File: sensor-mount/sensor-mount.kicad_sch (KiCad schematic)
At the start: 6 parts, among them J1 Conn_01x02, J2 Conn_01x02, U1 MAX31725

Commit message: The Maxim footprint has 0.65mm pitch.
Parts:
- U1: footprint Package_DFN_QFN:TDFN-8-1EP_3x2mm_P0.5mm_EP1.80x1.65mm_ThermalVias -> maxim-8tdfn-vias:DFN-8-1EP_3x3mm_P0.65mm_EP1.7x2.05mm
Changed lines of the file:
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@@
     (property "Reference" "U1" (id 0) (at 134.62 87.63 0))
     (property "Value" "MAX31725" (id 1) (at 134.62 81.28 0))
-    (property "Footprint" "Package_DFN_QFN:TDFN-8-1EP_3x2mm_P0.5mm_EP1.80x1.65mm_ThermalVias" (id 2) (at 134.62 87.63 0)
+    (property "Footprint" "maxim-8tdfn-vias:DFN-8-1EP_3x3mm_P0.65mm_EP1.7x2.05mm" (id 2) (at 134.62 87.63 0)
       (effects (font (size 1.27 1.27)) hide)
     )
@@
     )
     (path "/1ccf6312-fd46-4669-9722-1b0a94926d20"
-      (reference "U1") (unit 1) (value "MAX31725") (footprint "Package_DFN_QFN:TDFN-8-1EP_3x2mm_P0.5mm_EP1.80x1.65mm_ThermalVias")
+      (reference "U1") (unit 1) (value "MAX31725") (footprint "maxim-8tdfn-vias:DFN-8-1EP_3x3mm_P0.65mm_EP1.7x2.05mm")
     )
   )

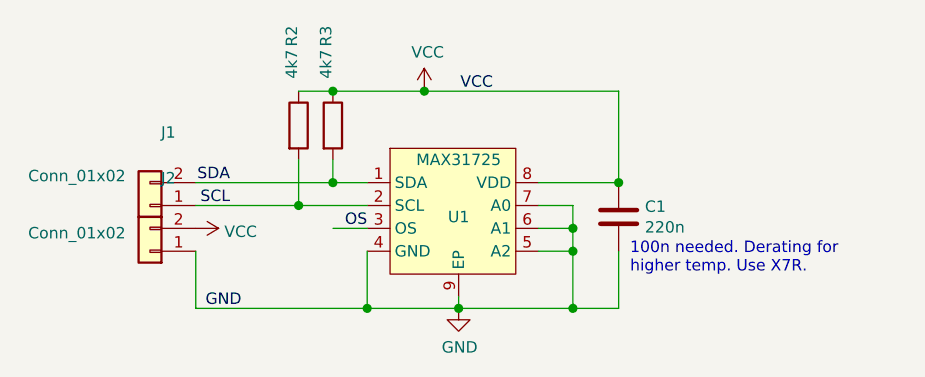
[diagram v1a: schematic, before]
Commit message: Upgrade to latest kicad; fix missing symbol library config.
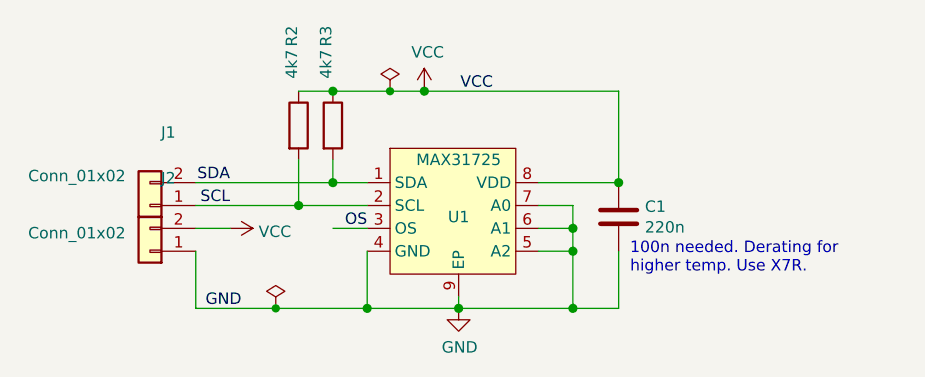
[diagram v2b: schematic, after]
